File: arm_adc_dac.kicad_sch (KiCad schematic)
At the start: 27 parts, among them J1 AudioJack2, J2 Conn_01x15, J3 Conn_01x15, P1 USB_C_Plug_USB2.0, U1 STM32F103C8Tx, U2 XC6206PxxxMR, U3 PCM1780, Y1 8MHz

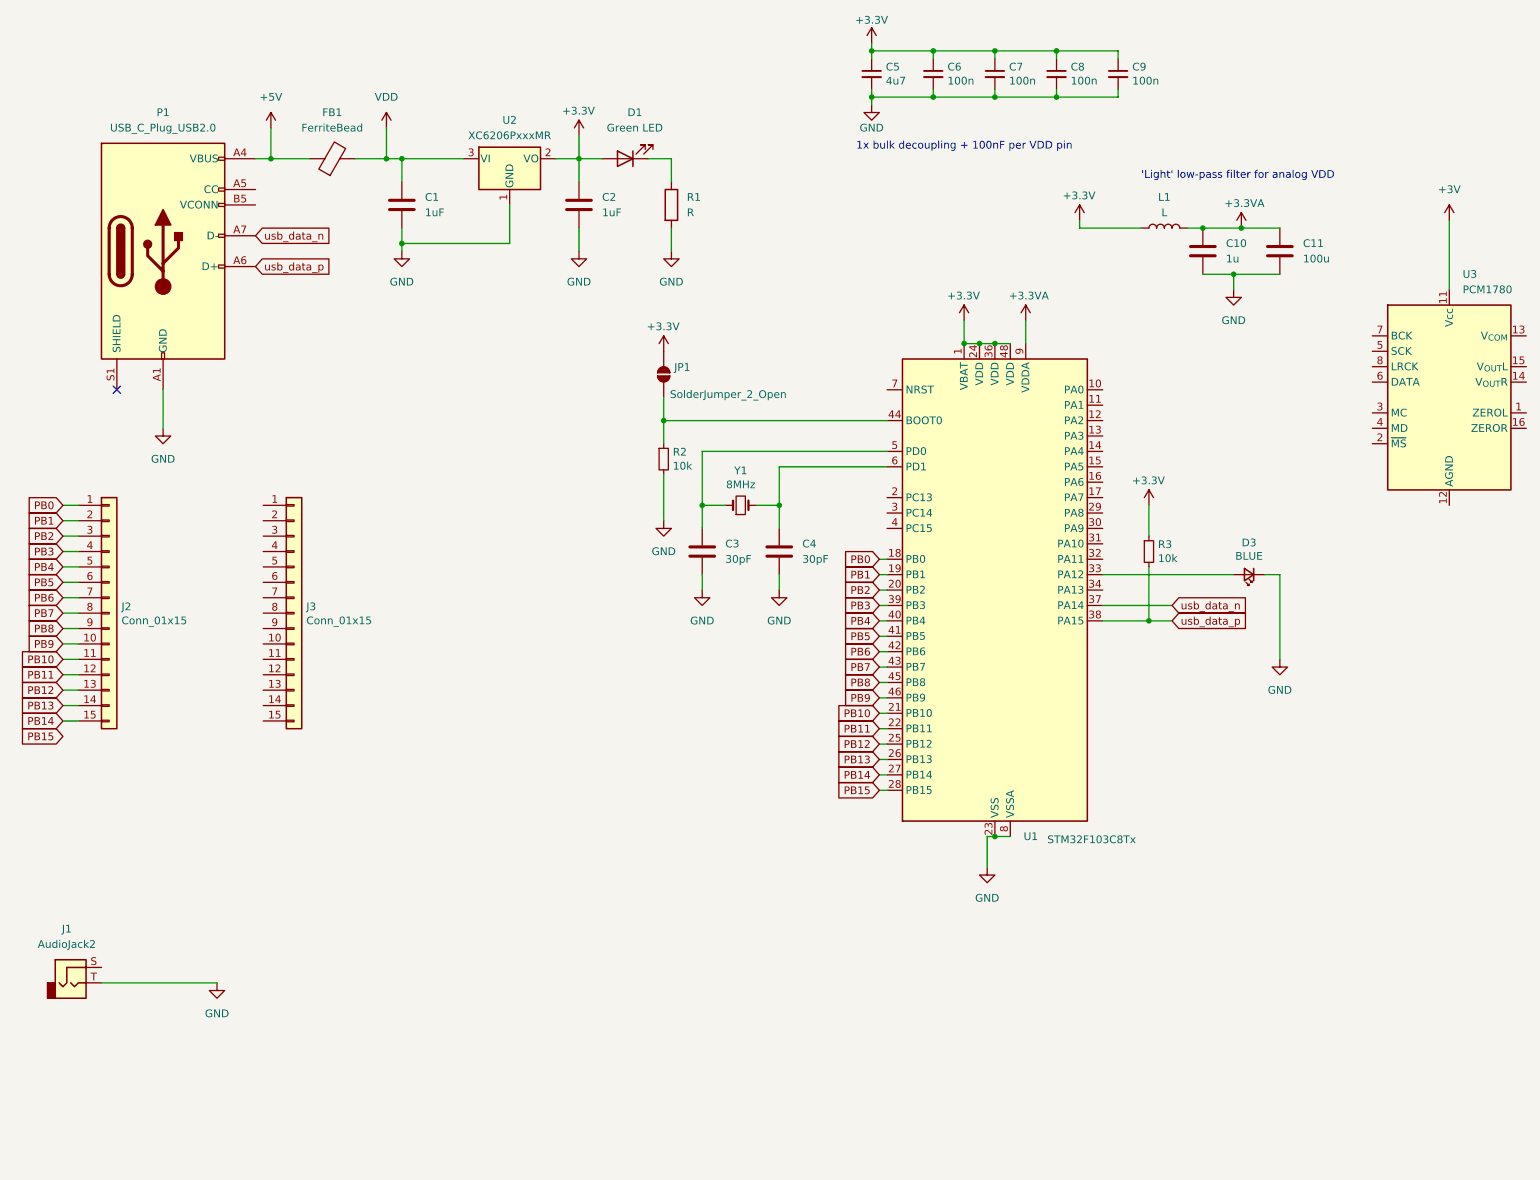
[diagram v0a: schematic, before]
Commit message: divide the schematic into sub sections, use 12 bit ADC/DAC, add schematic
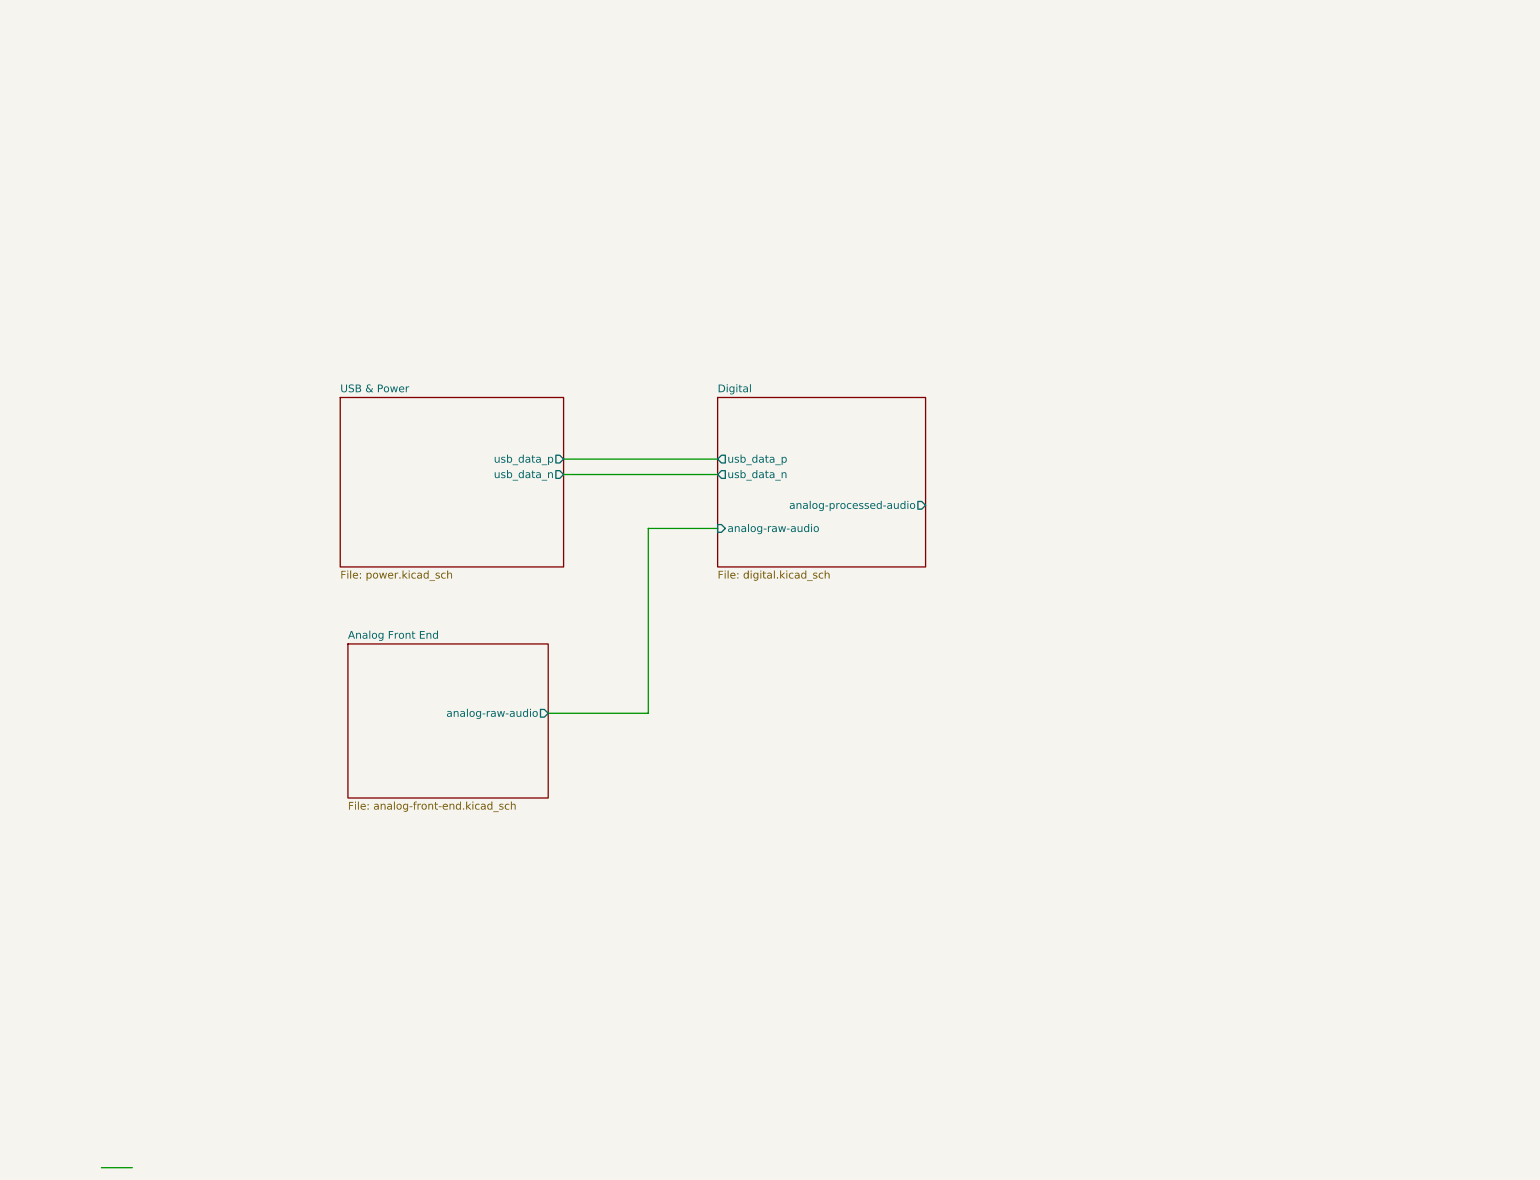
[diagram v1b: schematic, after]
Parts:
- removed C1, C2: 1uF, symbol Device:C
- removed C10: 1u, symbol Device:C
- removed C11: 100u, symbol Device:C
- removed C3, C4: 30pF, symbol Device:C
- removed C5: 4u7, Capacitor_SMD:C_0603_1608Metric, symbol Device:C_Small
- removed C6, C7, C8, C9: 100n, Capacitor_SMD:C_0402_1005Metric, symbol Device:C_Small
- removed D1: Green LED, symbol Device:LED
- removed D3: BLUE, LED_SMD:LED_0603_1608Metric, symbol Device:LED_Small
- removed FB1: FerriteBead, symbol Device:FerriteBead
- removed J1: AudioJack2, Connector_Audio:Jack_3.5mm_CUI_SJ1-3523N_Horizontal, symbol Connector_Audio:AudioJack2
- removed J2, J3: Conn_01x15, Connector_PinHeader_2.54mm:PinHeader_1x15_P2.54mm_Vertical, symbol Connector_Generic:Conn_01x15
- removed JP1: SolderJumper_2_Open, Jumper:SolderJumper-2_P1.3mm_Open_Pad1.0x1.5mm, symbol Jumper:SolderJumper_2_Open
- removed L1: L, symbol Device:L
- removed P1: USB_C_Plug_USB2.0, Connector_USB:USB3_A_Molex_48393-001, symbol Connector:USB_C_Plug_USB2.0
- removed R1: R, symbol Device:R
- removed R2, R3: 10k, Resistor_SMD:R_0402_1005Metric, symbol Device:R_Small
- removed U1: STM32F103C8Tx, Package_QFP:LQFP-48_7x7mm_P0.5mm, symbol MCU_ST_STM32F1:STM32F103C8Tx
- removed U2: XC6206PxxxMR, Package_TO_SOT_SMD:SOT-23-3, symbol Regulator_Linear:XC6206PxxxMR
- removed U3: PCM1780, Package_SO:SSOP-16_3.9x4.9mm_P0.635mm, symbol Audio:PCM1780
- removed Y1: 8MHz, Crystal:Crystal_SMD_5032-2Pin_5.0x3.2mm, symbol Device:Crystal_Small
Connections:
- no-connect marks 1 -> 0
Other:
- added sheet Analog Front End (analog-front-end.kicad_sch)
- added sheet Digital (digital.kicad_sch)
- added sheet USB & Power (power.kicad_sch)
- note removed: "'Light' low-pass filter for analog VDD"
- note removed: "1x bulk decoupling + 100nF per VDD pin"
